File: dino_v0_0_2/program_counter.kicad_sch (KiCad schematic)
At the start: 20 parts, among them U1 74LS193, U10 74LS02, U11 74LS245, U12 74LS245, U13 74LS245, U14 74LS245, U2 74LS193, U3 74LS193, U36 7400, U4 74LS193

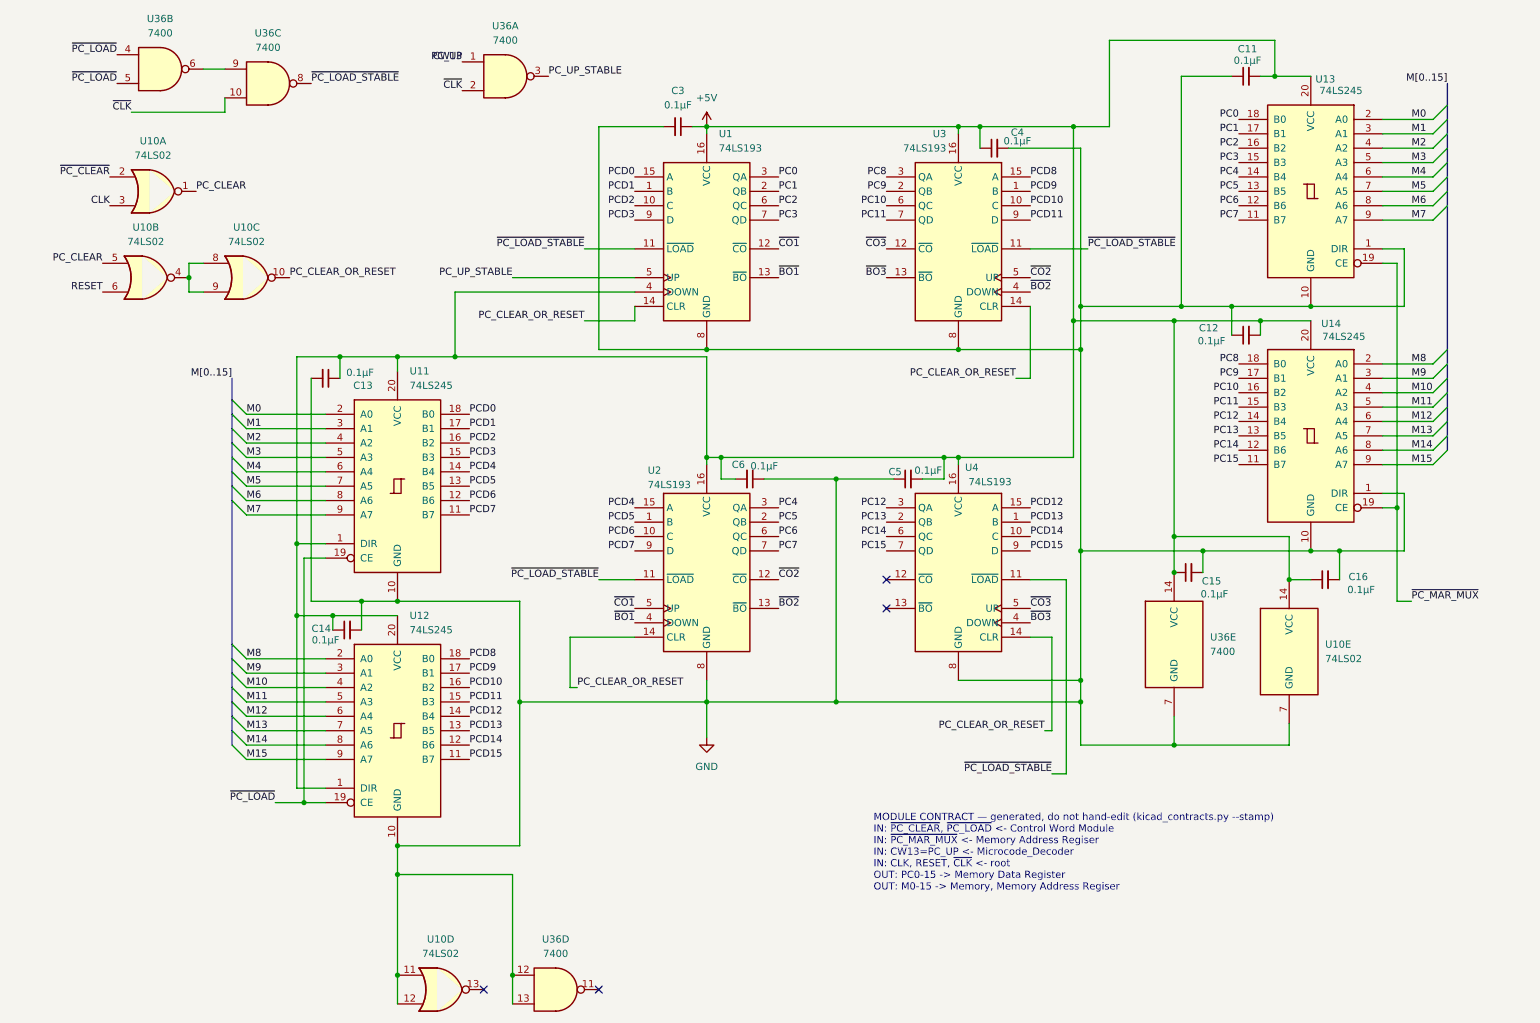
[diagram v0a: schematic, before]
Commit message: feat(kicad): footprints, power sheet, global labels, PCB draft
Every symbol gets a stock THT footprint (plain DIP, no sockets, so the
3D render shows ICs). New Power sheet: 24-pin ATX header for a picoPSU,
rails +5V/+3.3V/+12V/-12V/GND only; no -5V exists on any ATX unit since
2003, none drawn. PS_ON# on a 2-pin header.

Cross-sheet labels become global labels. KiCad joined nothing between
sheets before: 122 base names were split per sheet, ERC saw 90 undriven
inputs whose driver sat one sheet away, and the PCB ratsnest stopped at
every sheet boundary. Proof: KiCad's netlist after equals a name-join of
its netlist before plus the 15 CW alias pairs, pin for pin.

kicad_contracts took a node's sheet from the net name's /Sheet/ prefix;
global nets have none, so it emitted an empty contracts doc. Sheet now
comes from the component's own path; the doc regenerates with zero diff.

ERC 477 -> 2. Real fixes: ROM I/O pins input -> tri_state, '382 GND pin
power_out -> power_in, four orphan symbols rehomed to project lib `dino`,
one stub wire. 133 by-design warnings excluded by uuid ('245 readback on
counter Q, alias stubs, probe-point labels); the two left are bus
signals the peripheral bus sheet will consume.

PCB draft: 198 footprints placed per sheet, all pads netted, no tracks.

Co-Authored-By: Claude Fable 5.1 <noreply@anthropic.com>
Claude-Session: https://claude.ai/code/session_018irreFHb1xEykW5kCD26ow
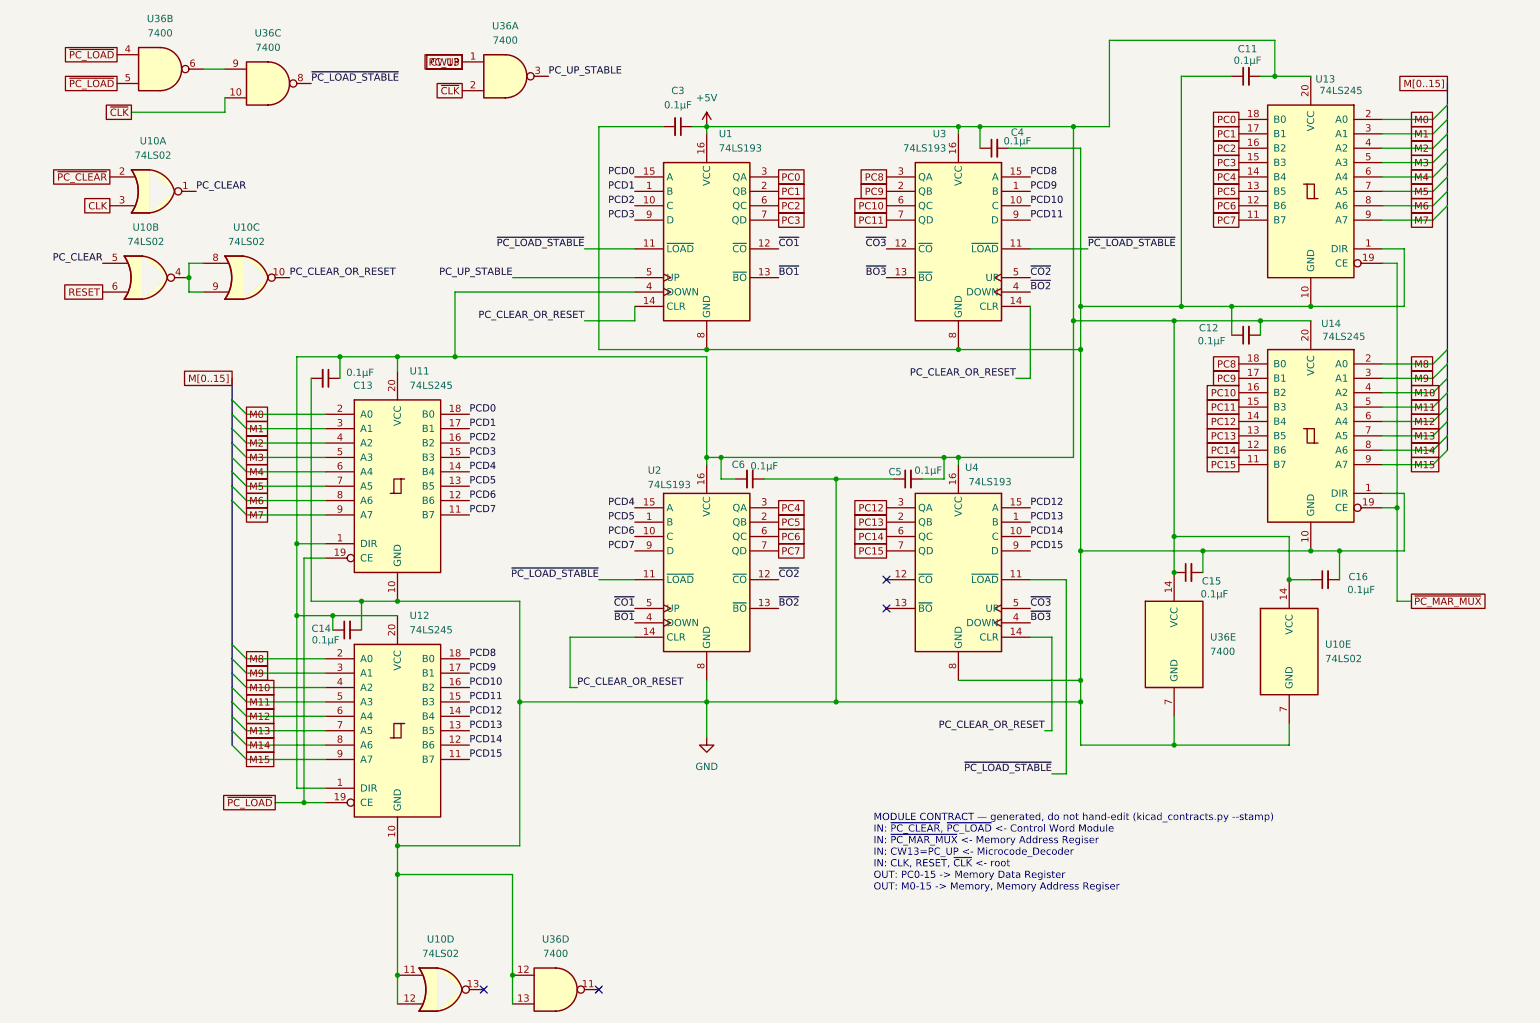
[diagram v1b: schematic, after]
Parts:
- C11, C12, C13, C14, C15, C16, C3, C4, C5, C6: footprint (none) -> Capacitor_THT:C_Disc_D5.0mm_W2.5mm_P2.50mm
- U1, U2, U3, U4: footprint (none) -> Package_DIP:DIP-16_W7.62mm
- U10, U36: footprint (none) -> Package_DIP:DIP-14_W7.62mm
- U11, U12, U13, U14: footprint (none) -> Package_DIP:DIP-20_W7.62mm
